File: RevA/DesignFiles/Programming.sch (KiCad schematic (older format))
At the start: 1 part

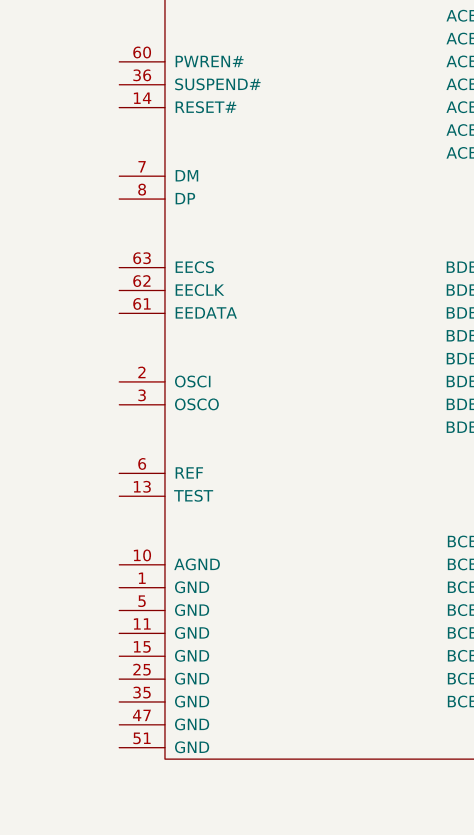
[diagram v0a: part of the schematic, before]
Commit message: placining heirarchy pins
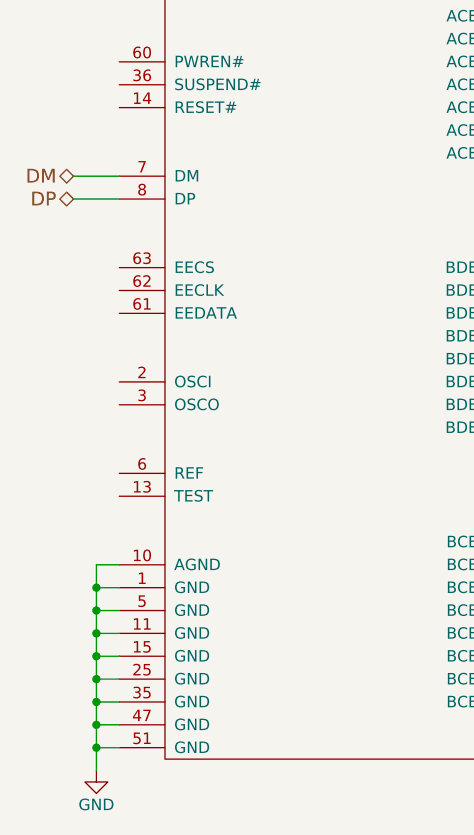
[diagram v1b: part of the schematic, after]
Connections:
- net GND: now reaches U?.1 (GND)
- net GND: now also U?.10 (AGND), U?.11 (GND), U?.15 (GND), U?.25 (GND), U?.35 (GND), U?.47 (GND), U?.5 (GND), U?.51 (GND)
- net DM: now reaches U?.7 (DM)
- net DP: now reaches U?.8 (DP)
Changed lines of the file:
@@
 	1    0    0    -1
 $EndComp
+Wire Wire Line
+	5050 3100 5250 3100
+Wire Wire Line
+	5050 3200 5250 3200
+Text HLabel 5050 3100 0    60   BiDi ~ 0
+DM
+Text HLabel 5050 3200 0    60   BiDi ~ 0
+DP
+Wire Wire Line
+	5250 5600 5150 5600
+Wire Wire Line
+	5150 4800 5150 5700
+Wire Wire Line
+	5150 4800 5250 4800
+Wire Wire Line
+	5250 4900 5150 4900
+Connection ~ 5150 4900
+Wire Wire Line
+	5250 5000 5150 5000
+Connection ~ 5150 5000
+Wire Wire Line
+	5250 5100 5150 5100
+Connection ~ 5150 5100
+Wire Wire Line
+	5250 5200 5150 5200
+Connection ~ 5150 5200
+Wire Wire Line
+	5250 5300 5150 5300
+Connection ~ 5150 5300
+Wire Wire Line
+	5250 5400 5150 5400
+Connection ~ 5150 5400
+Wire Wire Line
+	5250 5500 5150 5500
+Connection ~ 5150 5500
+$Comp
+L GND #PWR?
+U 1 1 5806CDC1
+P 5150 5700
+F 0 "#PWR?" H 5150 5450 50  0001 C CNN
+F 1 "GND" H 5150 5550 50  0000 C CNN
+F 2 "" H 5150 5700 50  0000 C CNN
+F 3 "" H 5150 5700 50  0000 C CNN
+	1    5150 5700
+	1    0    0    -1
+$EndComp
+Connection ~ 5150 5600
 $EndSCHEMATC

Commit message: more psu stuff for ftdi
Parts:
- added C? (x3): 100nF, symbol C
- added C?: 10uF, symbol C
- added C? (x2): 4.7uF, symbol C
- added R?: 2.2K, symbol R
- added R?: 12K, symbol R
- added R? (x4): 10K, symbol R
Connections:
- net labels added: +1V8, +3V3
- wire segments 12 -> 65
- no-connect marks 0 -> 19
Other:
- moved on the sheet: U?
